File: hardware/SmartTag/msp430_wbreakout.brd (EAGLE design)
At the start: 32.7 x 40.6 mm, 16 parts, among them U1 ADXL362

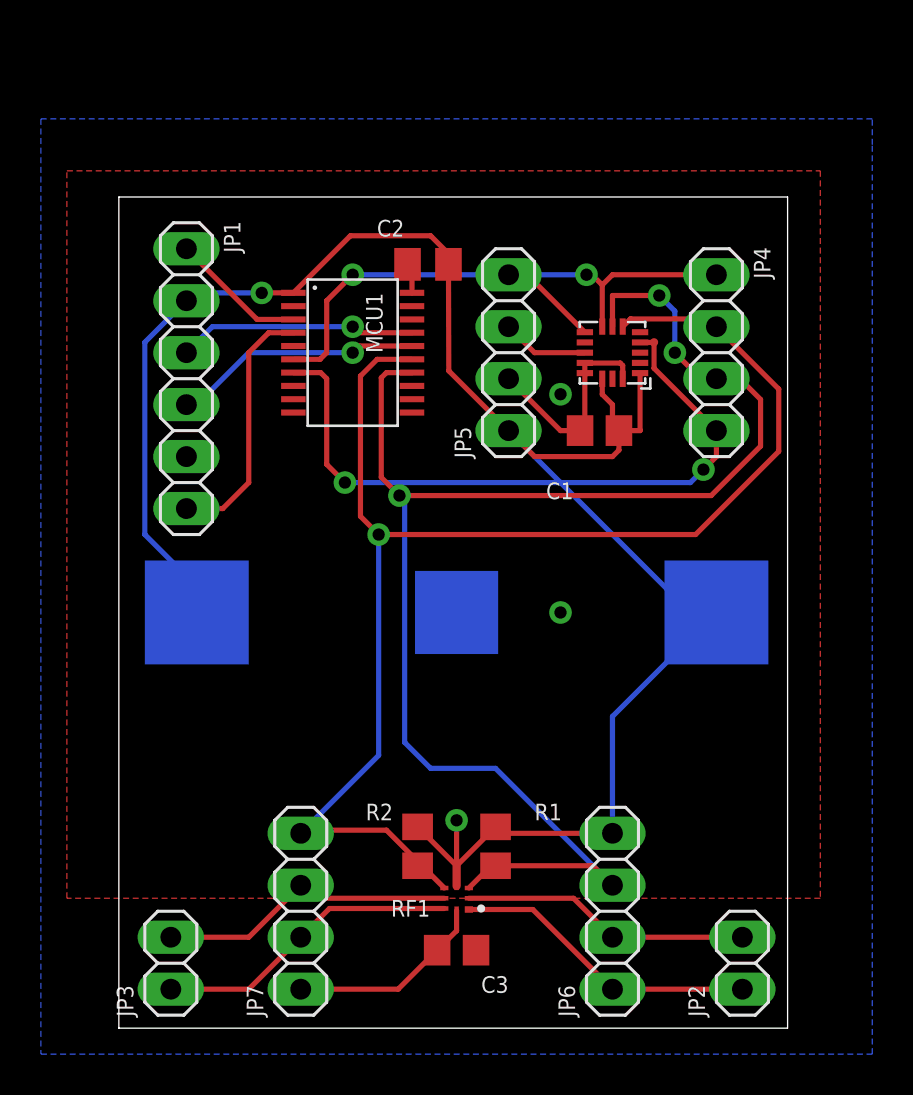
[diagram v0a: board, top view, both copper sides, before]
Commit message: hw: Add status LED and capacitive sensor headers
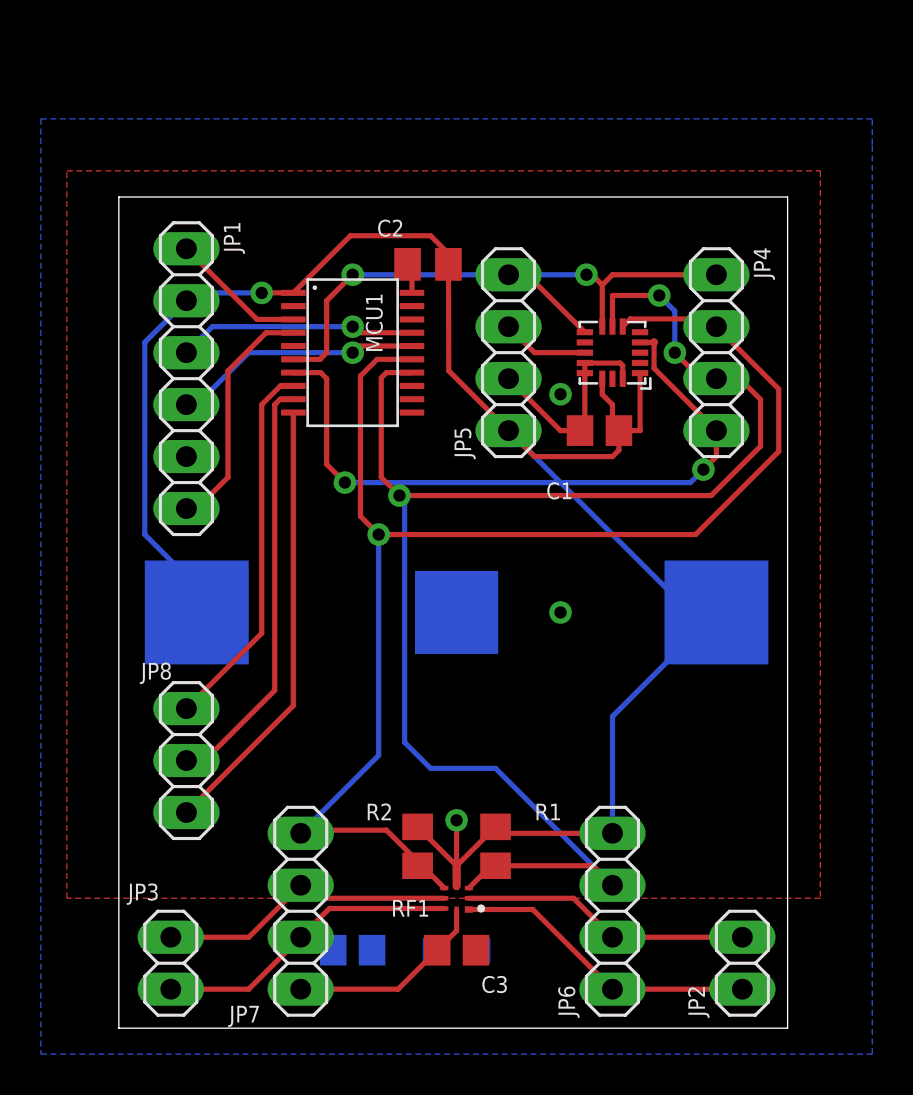
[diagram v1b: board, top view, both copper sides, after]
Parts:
- added JP8: (no value), pinhead:1X03
- added LED1: (no value), led:CHIP-LED0805
- added R3: 470k, rcl:R0805
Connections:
- new net N$1: LED1.A, R3.2
- new net P2.3: R3.1
- net GND: now also LED1.C
- net P2.0: now also JP8.1
- net P2.1: now also JP8.2
- net P2.2: now also JP8.3
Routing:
- net P2.2: track 0.00 -> 21.7 mm
- net P2.1: track 0.00 -> 20.7 mm
- net P2.0: track 0.00 -> 18.3 mm
- net P1.2/TX: track 12.5 -> 11.8 mm
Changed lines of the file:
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@@
 </element>
 <element name="JP3" library="pinhead" package="1X02" value="" x="2.54" y="1.905" smashed="yes" rot="R90">
-<attribute name="NAME" x="0.7112" y="-0.7112" size="0.8128" layer="25" ratio="10" rot="R90"/>
+<attribute name="NAME" x="1.9812" y="5.7912" size="0.8128" layer="25" ratio="10" rot="R180"/>
 <attribute name="VALUE" x="5.715" y="-0.635" size="1.27" layer="27" rot="R90"/>
 </element>
@@
 </element>
 <element name="JP7" library="pinhead" package="1X04" value="" x="8.89" y="4.445" smashed="yes" rot="R90">
-<attribute name="NAME" x="7.0612" y="-0.7112" size="0.8128" layer="25" ratio="10" rot="R90"/>
+<attribute name="NAME" x="6.9342" y="-0.1778" size="0.8128" layer="25" ratio="10" rot="R180"/>
 <attribute name="VALUE" x="12.065" y="-0.635" size="1.27" layer="27" rot="R90"/>
+</element>
+<element name="LED1" library="led" package="CHIP-LED0805" value="" x="16.51" y="2.54" smashed="yes" rot="MR90">
+<attribute name="NAME" x="15.24" y="1.27" size="0.8128" layer="26" rot="MR180"/>
+<attribute name="VALUE" x="15.24" y="5.08" size="1.27" layer="28" rot="MR180"/>
+</element>
+<element name="R3" library="rcl" package="R0805" value="470k" x="11.43" y="2.54" smashed="yes" rot="MR180">
+<attribute name="NAME" x="10.795" y="1.27" size="0.8128" layer="26" rot="MR180"/>
+</element>
+<element name="JP8" library="pinhead" package="1X03" value="" x="3.302" y="11.811" smashed="yes" rot="R270">
+<attribute name="NAME" x="2.6162" y="16.5862" size="0.8128" layer="25" ratio="10" rot="R180"/>
+<attribute name="VALUE" x="0.127" y="15.621" size="1.27" layer="27" rot="R270"/>
 </element>
 </elements>
@@
 <contactref element="MCU1" pad="4"/>
 <contactref element="JP1" pad="6"/>
-<wire x1="8.5299" y1="32.725" x2="7.325" y2="32.725" width="0.254" layer="1"/>
-<wire x1="7.325" y1="32.725" x2="6.35" y2="31.75" width="0.254" layer="1"/>
-<wire x1="6.35" y1="31.75" x2="6.35" y2="25.4" width="0.254" layer="1"/>
-<wire x1="6.35" y1="25.4" x2="5.08" y2="24.13" width="0.254" layer="1"/>
-<wire x1="3.302" y1="24.13" x2="5.08" y2="24.13" width="0.254" layer="1"/>
+<wire x1="3.302" y1="24.13" x2="3.81" y2="24.13" width="0.254" layer="1"/>
+<wire x1="3.81" y1="24.13" x2="5.334" y2="25.654" width="0.254" layer="1"/>
+<wire x1="5.334" y1="25.654" x2="5.334" y2="30.861" width="0.254" layer="1"/>
+<wire x1="5.334" y1="30.861" x2="7.198" y2="32.725" width="0.254" layer="1"/>
+<wire x1="7.198" y1="32.725" x2="8.5299" y2="32.725" width="0.254" layer="1"/>
 </signal>
 <signal name="P1.3/NC">
@@
 <signal name="P2.0">
 <contactref element="MCU1" pad="8"/>
+<contactref element="JP8" pad="1"/>
+<wire x1="8.5299" y1="30.125" x2="7.9" y2="30.125" width="0.254" layer="1"/>
+<wire x1="7.9" y1="30.125" x2="6.985" y2="29.21" width="0.254" layer="1"/>
+<wire x1="6.985" y1="29.21" x2="6.985" y2="18.034" width="0.254" layer="1"/>
+<wire x1="6.985" y1="18.034" x2="3.302" y2="14.351" width="0.254" layer="1"/>
 </signal>
 <signal name="P2.1">
 <contactref element="MCU1" pad="9"/>
+<contactref element="JP8" pad="2"/>
+<wire x1="3.302" y1="11.811" x2="4.191" y2="11.811" width="0.254" layer="1"/>
+<wire x1="4.191" y1="11.811" x2="7.62" y2="15.24" width="0.254" layer="1"/>
+<wire x1="7.62" y1="15.24" x2="7.62" y2="29.21" width="0.254" layer="1"/>
+<wire x1="7.62" y1="29.21" x2="7.885" y2="29.475" width="0.254" layer="1"/>
+<wire x1="7.885" y1="29.475" x2="8.5299" y2="29.475" width="0.254" layer="1"/>
 </signal>
 <signal name="P2.2">
 <contactref element="MCU1" pad="10"/>
+<contactref element="JP8" pad="3"/>
+<wire x1="8.5299" y1="28.8251" x2="8.5299" y2="14.4989" width="0.254" layer="1"/>
+<wire x1="8.5299" y1="14.4989" x2="3.302" y2="9.271" width="0.254" layer="1"/>
 </signal>
 <signal name="DVSS">
@@
 <via x="21.59" y="19.05" extent="1-16" drill="0.6"/>
 <via x="21.59" y="29.718" extent="1-16" drill="0.6"/>
+<contactref element="LED1" pad="C"/>
 </signal>
 <signal name="RF1P">
@@
 <wire x1="19.97" y1="35.56" x2="19.05" y2="35.56" width="0.254" layer="1"/>
 </signal>
+<signal name="N$1">
+<contactref element="R3" pad="2"/>
+<contactref element="LED1" pad="A"/>
+<wire x1="12.38" y1="2.54" x2="15.46" y2="2.54" width="0" layer="19" extent="16-16"/>
+</signal>
+<signal name="P2.3">
+<contactref element="R3" pad="1"/>
+</signal>
 </signals>

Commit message: hw: Add LED to schematic and board.
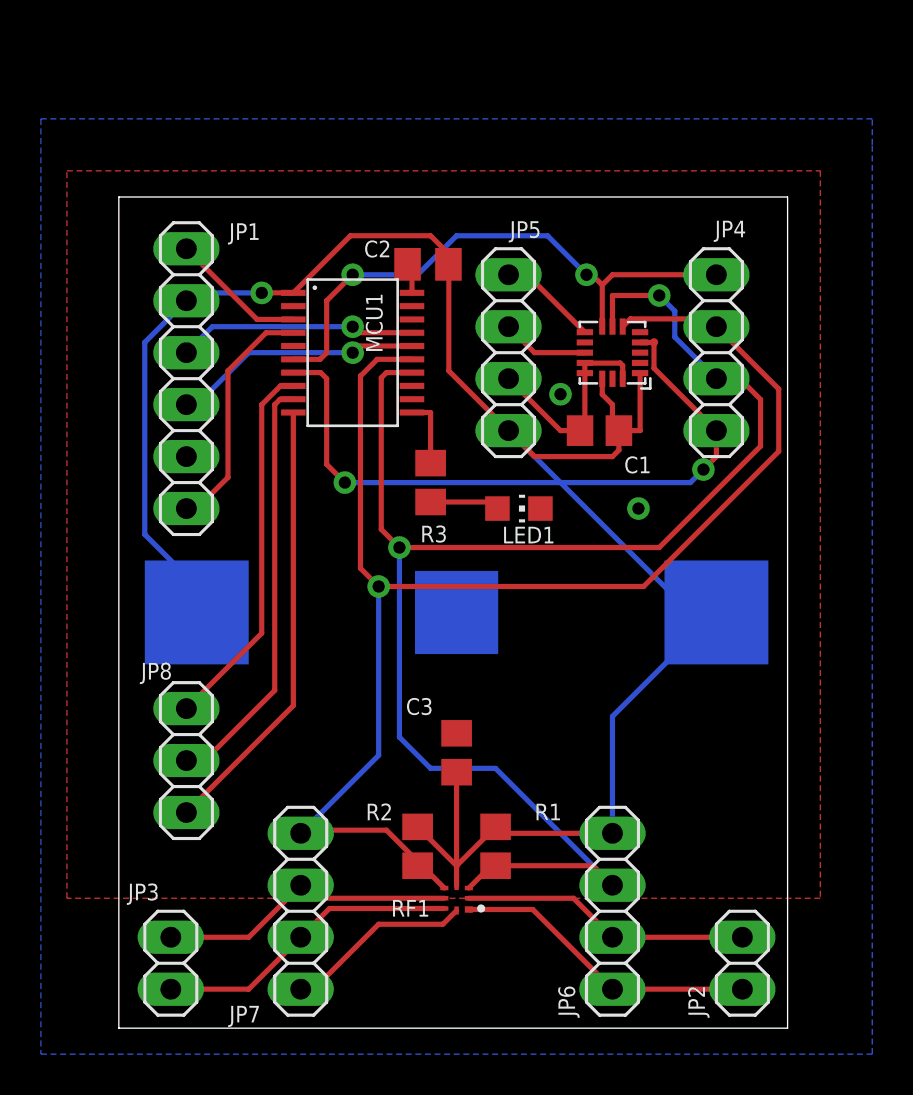
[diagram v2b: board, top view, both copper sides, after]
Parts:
- moved R3 23.2 mm to (15.2, 25.4), flipped to the top, turned to 270 degrees
- moved LED1 21.8 mm to (19.6, 24.1), flipped to the top, turned to 270 degrees
- moved C3 9.65 mm to (16.5, 12.2), turned to 90 degrees
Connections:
- removed net P2.3/NC: MCU1.11
- net P2.3: now also MCU1.11
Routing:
- net N$1: track 0.00 -> 3.40 mm
- net P2.3: track 0.00 -> 3.39 mm
- net P1.4: track 26.3 -> 27.9 mm
- net VCC: track 99.2 -> 100.5 mm, vias 2 -> 1
- net P1.7: track 69.1 -> 70.2 mm
- net P1.6: track 73.8 -> 74.4 mm, vias 3 -> 2
- net GND: track 22.1 -> 21.5 mm

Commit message: hw: Update based on 1/29 Meeting Notes
Added pin header for Bluetooth board.
Added RESET switch.
Rearranged traces for capacitive sensor connections.

Passed DRC and ERC using SparkFun "Tight" rules
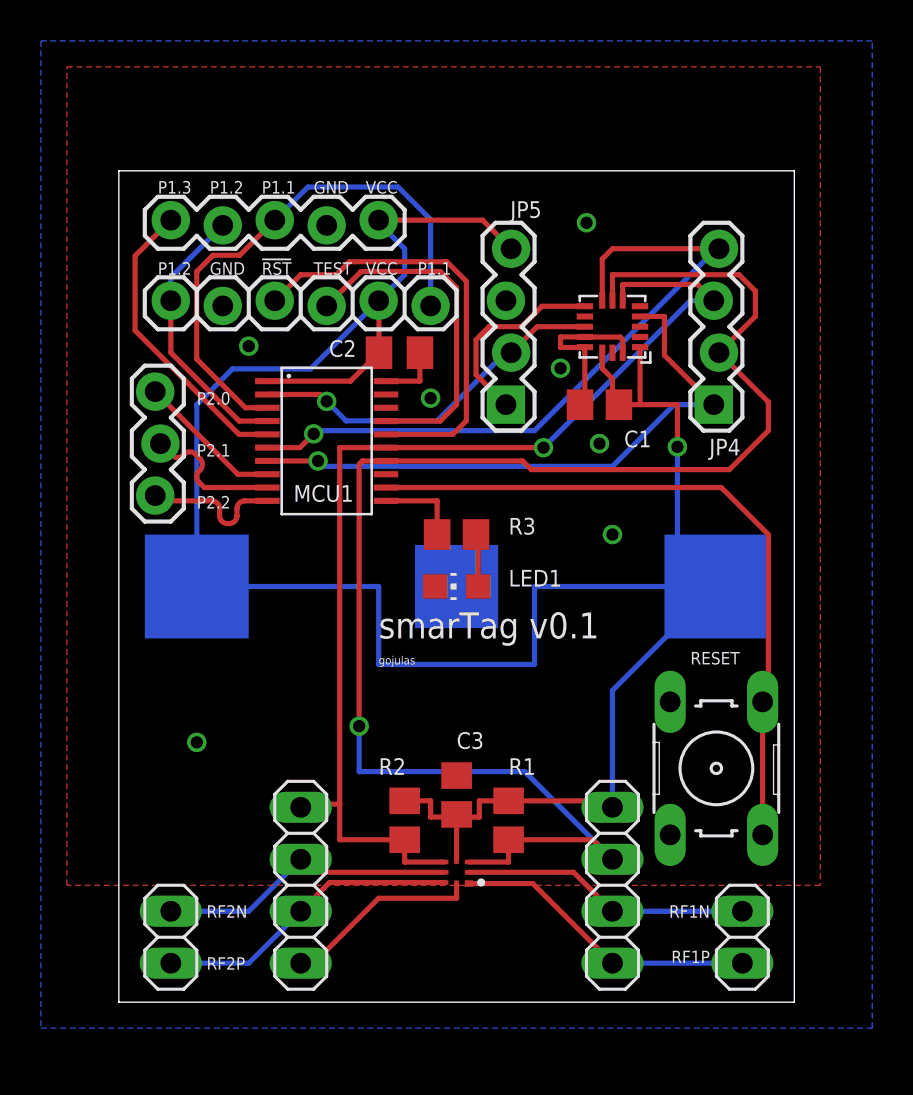
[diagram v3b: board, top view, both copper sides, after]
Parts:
- added JP9: (no value), SparkFun-Connectors:1X05_LOCK
- added S1: (no value), switch-omron:B3F-10XX
- C1, C2, C3: value (none) -> 0.1uF
- JP1: device pinhead:1X06 -> SparkFun-Connectors:1X06_LOCK
- JP4, JP5: device pinhead:1X04 -> SparkFun-Connectors:1X04_LOCK
- JP8: device pinhead:1X03 -> SparkFun-Connectors:1X03_LOCK
- R1, R2: value (none) -> 270k
- R3: value 470k -> 470
- moved JP8 13.0 mm to (1.91, 24.8), turned to 90 degrees
- moved LED1 4.88 mm to (16.5, 20.3), turned to 90 degrees
- moved C2 4.54 mm to (13.7, 31.8), turned to 0 degrees
- moved MCU1 4.50 mm to (10.2, 27.4)
- moved JP1 3.89 mm to (2.54, 34.3), turned to 0 degrees
- moved R3 2.84 mm to (16.5, 22.9), turned to 0 degrees
- moved JP4 2.54 mm to (29.2, 29.2), turned to 90 degrees
- moved JP5 2.54 mm to (19.1, 29.2)
- moved C3 2.06 mm to (16.5, 10.1)
- moved R1 1.42 mm to (19.1, 8.89)
- moved R2 1.42 mm to (14.0, 8.89)
- moved U1 1.27 mm to (24.1, 33.0)
- moved JP2 1.27 mm to (30.5, 3.17)
- moved JP3 1.27 mm to (2.54, 3.17)
- moved BATT 1.27 mm to (16.5, 20.3)
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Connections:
- net N$12 renamed P2.6/NC
- net N$13 renamed P2.7/NC
- net P2.1 renamed P2.1_C
- removed net P1.1: JP5.3, U1.P$11
- removed net P1.3/NC: MCU1.5
- removed net P2.0: JP8.1, MCU1.8
- removed net P2.2: JP8.3, MCU1.10
- removed net P2.4/NC: MCU1.12
- new net P1.3: JP9.1, MCU1.5
- new net P2.0_C: JP8.3, MCU1.8
- new net P2.2_C: JP8.1, MCU1.10
- new net P2.4: MCU1.12, S1.3, S1.4
- net !RST: now also JP1.3; no longer JP1.4
- net GND: now also JP1.2, JP5.3, JP9.4, S1.1, S1.2; no longer JP1.5, JP5.2
- net INT2: now also JP5.1; no longer JP5.4
- net P1.0: now also JP5.2, U1.P$11
- net P1.1/RX: now also JP1.6, JP9.3; no longer JP1.1
- net P1.2/TX: now also JP1.1, JP9.2; no longer JP1.6
- net P1.4: now also JP4.4; no longer JP4.1
- net P1.5: now also JP4.1; no longer JP4.4
- net P1.6: now also JP4.2; no longer JP4.3
- net P1.7: now also JP4.3; no longer JP4.2
- net TEST: now also JP1.4; no longer JP1.3
- net VCC: now also JP1.5, JP5.4, JP9.5; no longer JP1.2, JP5.1
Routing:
- net P2.4: track 0.00 -> 34.4 mm
- net P2.2: track 21.7 -> 0.00 mm
- net P1.1/RX: track 6.66 -> 26.7 mm
- net VCC: track 100.5 -> 119.1 mm
- net P2.0: track 18.3 -> 0.00 mm
- net P1.0: track 0.00 -> 18.0 mm, vias 0 -> 1
- net P1.7: track 70.2 -> 54.2 mm
- net P1.3: track 0.00 -> 14.7 mm
- net P2.1_C: track 20.7 -> 6.92 mm
- net !RST: track 12.2 -> 21.6 mm, vias 1 -> 0
- net P2.0_C: track 0.00 -> 7.15 mm
- net P2.2_C: track 0.00 -> 6.92 mm
- net P1.4: track 27.9 -> 34.1 mm, vias 2 -> 1
- net TEST: track 11.7 -> 16.9 mm, vias 1 -> 0
- net INT2: track 4.89 -> 9.77 mm
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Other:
- board size 32.7 x 40.6 mm -> 33 x 40.6 mm
- board text added: "!RST"
- board text added: "GND"
- board text added: "P1.1"
- board text added: "P1.2"
- board text added: "P1.3"
- board text added: "P2.0"
- board text added: "P2.1"
- board text added: "P2.2"
- board text added: "RESET"
- board text added: "RF1N"
- board text added: "RF1P"
- board text added: "RF2N"
- board text added: "RF2P"
- board text added: "TEST"
- board text added: "VCC"
- board text added: "gojulas"
- board text added: "smarTag v0.1"

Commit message: hw: Rework a few traces.
Rerouted some traces to remove sharp turns/angles.

Passed ERC and DRC
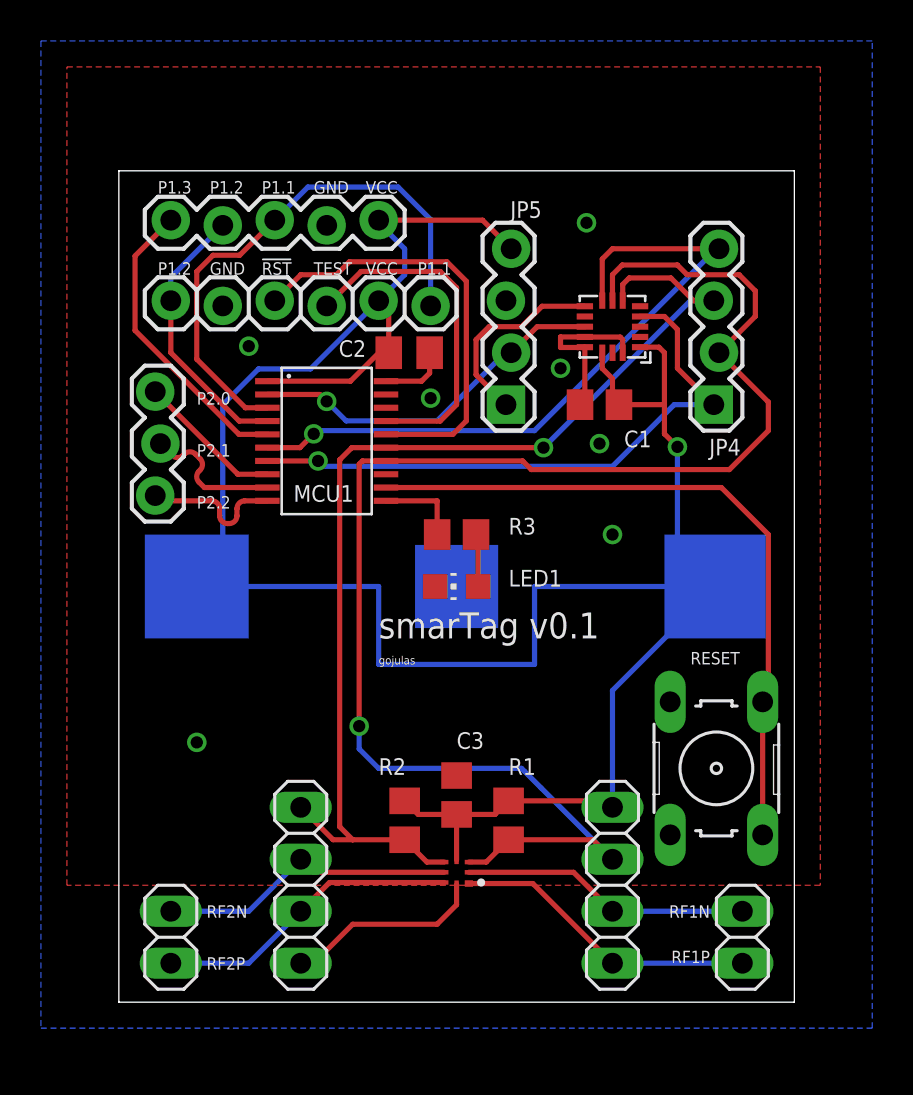
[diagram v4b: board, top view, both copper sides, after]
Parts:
- moved C2 0.48 mm to (14.2, 31.8)
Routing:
- net P1.6: track 75.9 -> 75.0 mm
- net VCC: track 119.1 -> 118.5 mm
